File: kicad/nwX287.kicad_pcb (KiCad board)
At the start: 2 copper layers, 18.3 x 31.1 mm, 5 parts, among them U1 bq4285, U2 socket, Y1 32.768kHz 6pF

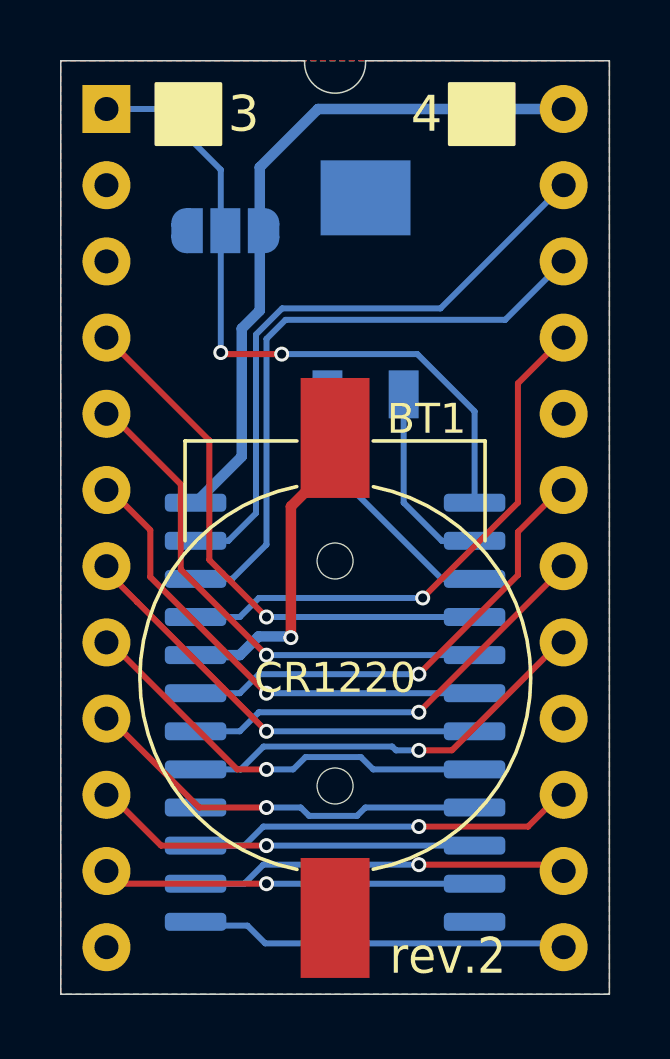
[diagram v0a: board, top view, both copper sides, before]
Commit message: CR2032 vertical holder and holes for easier oscillator mount
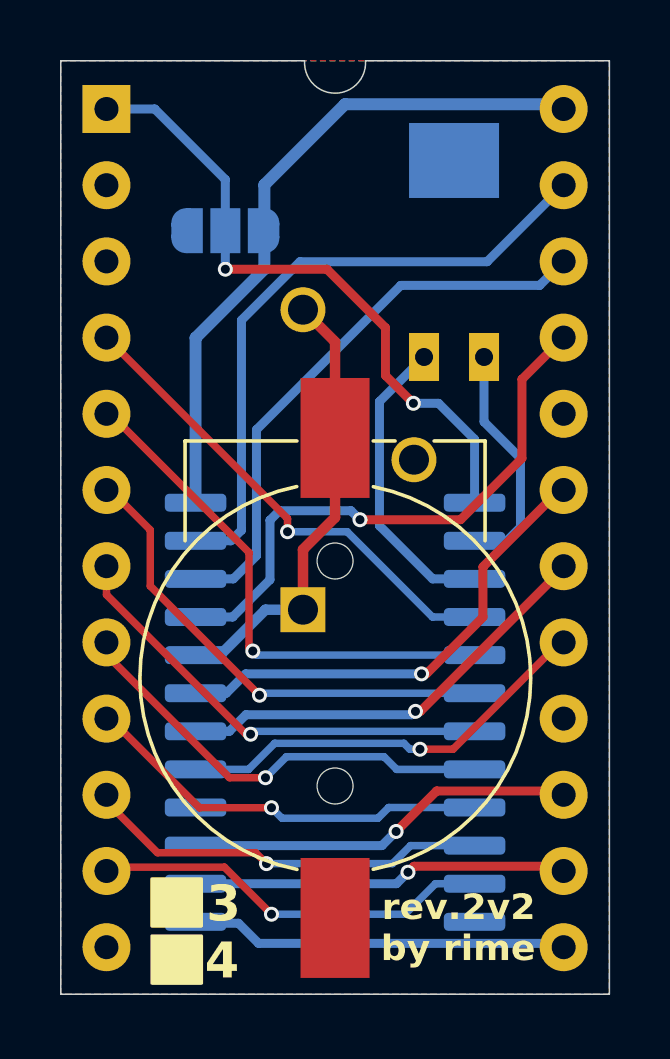
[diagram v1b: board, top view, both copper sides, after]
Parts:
- added BT2: 2032, Rime:CR2032_Vertical, F.Cu at (135.4, 91.2)
- BT1: value CR1220 -> 1220
- moved Y1 3.20 mm to (138.6, 84.2)
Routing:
- net BC: track 10.7 -> 15.1 mm, vias 1 -> 0
- net AD0: track 18.5 -> 16.4 mm
- net CEO: track 20.7 -> 19.1 mm
- net VOUT: track 23.1 -> 21.6 mm
- net X1: track 6.50 -> 7.89 mm
- net X2: track 8.82 -> 10.1 mm
- net AD7: track 12.5 -> 13.3 mm
- net AD6: track 13.0 -> 13.7 mm
- net CEI: track 18.5 -> 19.1 mm
- net SQW: track 20.7 -> 21.3 mm
- net AD4: track 14.4 -> 15.0 mm
- net AD3: track 14.8 -> 15.3 mm
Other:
- board text added: "1"
- board text added: "Force mode default is open"
- board text added: "rev.${REVISION}v2 by rime"
- board text removed: "rev.${REVISION}"
